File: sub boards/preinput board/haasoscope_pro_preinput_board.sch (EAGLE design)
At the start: 31 parts, among them J4 8pin, K1 G6K-2F-RF-T-TR03_DC5, K2 G6K-2F-RF-T-TR03_DC5, K3 TLP3475R_TP,F, K5 G6K-2F-RF-T-TR03_DC5, Q1 S8050, Q2 S8050, Q3 S8050

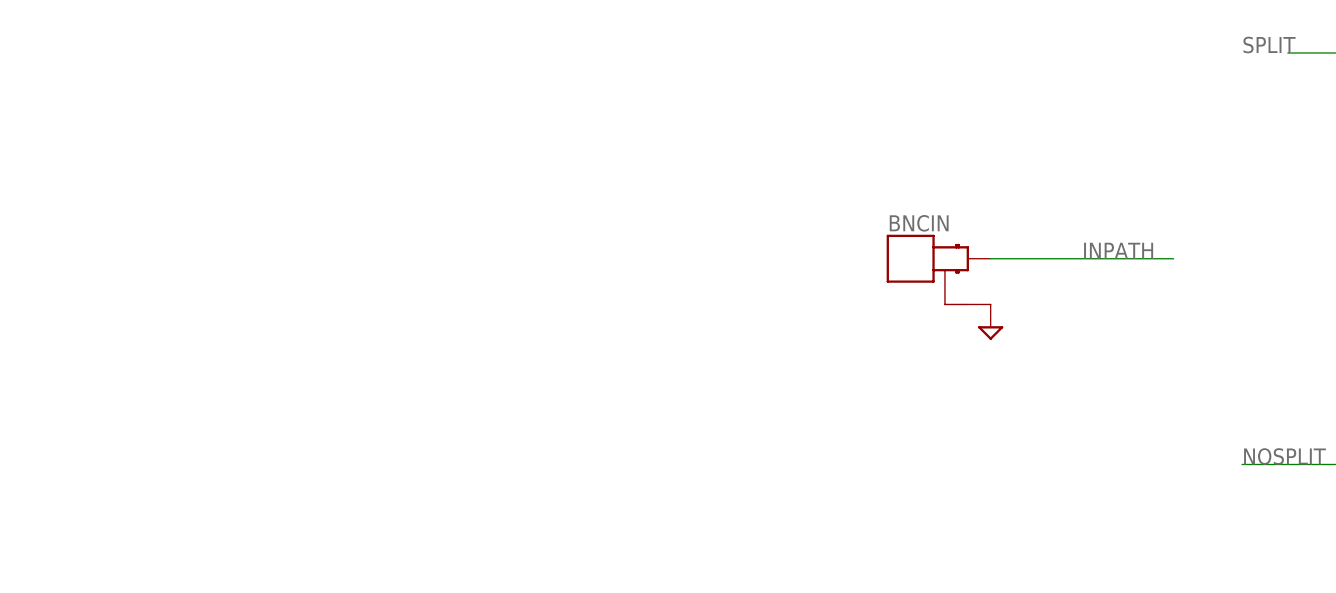
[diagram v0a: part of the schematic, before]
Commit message: Deemphasis filter
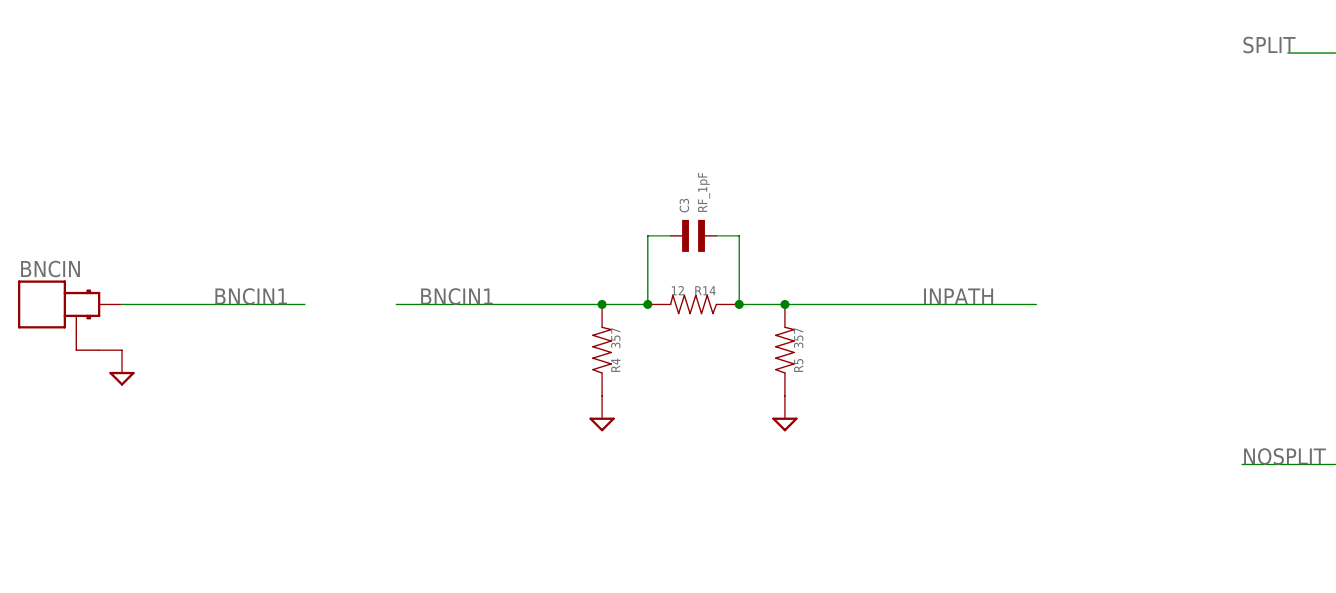
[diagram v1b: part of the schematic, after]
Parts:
- added C3: RF_1pF, MF_Passives:CAPACITOR_NP_0402
- added R14: 12, MF_Passives:RESISTOR_0402
- added R4, R5: 357, MF_Passives:RESISTOR_0402
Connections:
- new net BNCIN1: BNCIN.SIGNAL, C3.P$1, R14.P$2, R4.P$2
- net GND: now also R4.P$1, R5.P$1
- net INPATH: now also C3.P$2, R14.P$1, R5.P$2; no longer BNCIN.SIGNAL
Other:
- note added: "Pre-deemphasis pi attenuator -2.2dB low F, -1.2dB high F RC cutoff at ~350 MHz 50 Ohm"
- moved on the sheet: BNCIN
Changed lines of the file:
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@@
 <part name="K2" library="G6K-2F-RF-T-TR03_DC5" deviceset="G6K-2F-RF-T-TR03_DC5" device=""/>
 <part name="SUPPLY16" library="supply2" library_urn="urn:adsk.eagle:library:372" deviceset="GND" device=""/>
+<part name="SUPPLY21" library="supply2" library_urn="urn:adsk.eagle:library:372" deviceset="GND" device=""/>
+<part name="SUPPLY22" library="supply2" library_urn="urn:adsk.eagle:library:372" deviceset="GND" device=""/>
+<part name="R4" library="MF_Passives" deviceset="RESISTOR" device="_0402" value="357"/>
+<part name="R5" library="MF_Passives" deviceset="RESISTOR" device="_0402" value="357"/>
+<part name="R14" library="MF_Passives" deviceset="RESISTOR" device="_0402" value="12"/>
+<part name="C3" library="MF_Passives" deviceset="CAPACITOR_NP" device="_0402" value="RF_1pF">
+<attribute name="LCSC" value="C52923"/>
+</part>
 </parts>
 <sheets>
@@
 for CL05A105KA5NQNC</text>
 <text x="142.24" y="-73.66" size="1.778" layer="90">Inputs and controls</text>
+<text x="68.58" y="76.2" size="1.778" layer="90">Pre-deemphasis pi attenuator
+-2.2dB low F, -1.2dB high F
+RC cutoff at ~350 MHz
+50 Ohm</text>
 </plain>
 <instances>
@@
 <attribute name="VALUE" x="308.61" y="79.502" size="1.778" layer="96" rot="R180"/>
 </instance>
-<instance part="BNCIN" gate="G$1" x="101.6" y="66.04" smashed="yes">
-<attribute name="MPN" x="109.22" y="66.04" size="1.778" layer="96" display="off"/>
-<attribute name="NAME" x="97.79" y="69.088" size="1.778" layer="95" ratio="12"/>
-</instance>
-<instance part="SUPPLY2" gate="GND" x="109.22" y="58.42" smashed="yes" rot="MR0"/>
+<instance part="BNCIN" gate="G$1" x="5.08" y="60.96" smashed="yes">
+<attribute name="MPN" x="12.7" y="60.96" size="1.778" layer="96" display="off"/>
+<attribute name="NAME" x="1.27" y="64.008" size="1.778" layer="95" ratio="12"/>
+</instance>
+<instance part="SUPPLY2" gate="GND" x="12.7" y="53.34" smashed="yes" rot="MR0"/>
 <instance part="SUPPLY3" gate="GND" x="439.42" y="73.66" smashed="yes" rot="MR0"/>
 <instance part="SUPPLY4" gate="GND" x="256.54" y="-7.62" smashed="yes"/>
@@
 </instance>
 <instance part="SUPPLY16" gate="GND" x="429.26" y="-7.62" smashed="yes"/>
+<instance part="SUPPLY21" gate="GND" x="66.04" y="48.26" smashed="yes"/>
+<instance part="SUPPLY22" gate="GND" x="86.36" y="48.26" smashed="yes"/>
+<instance part="R4" gate="G$1" x="66.04" y="55.88" smashed="yes" rot="R180">
+<attribute name="NAME" x="67.056" y="53.34" size="1.016" layer="95" font="vector" rot="R90" align="top-left"/>
+<attribute name="VALUE" x="67.056" y="58.42" size="1.016" layer="96" font="vector" rot="R270"/>
+</instance>
+<instance part="R5" gate="G$1" x="86.36" y="55.88" smashed="yes" rot="R180">
+<attribute name="NAME" x="87.376" y="53.34" size="1.016" layer="95" font="vector" rot="R90" align="top-left"/>
+<attribute name="VALUE" x="87.376" y="58.42" size="1.016" layer="96" font="vector" rot="R270"/>
+</instance>
+<instance part="R14" gate="G$1" x="76.2" y="60.96" smashed="yes" rot="R270">
+<attribute name="NAME" x="78.74" y="61.976" size="1.016" layer="95" font="vector" rot="R180" align="top-left"/>
+<attribute name="VALUE" x="73.66" y="61.976" size="1.016" layer="96" font="vector"/>
+</instance>
+<instance part="C3" gate="G$1" x="76.2" y="68.58" smashed="yes" rot="R90">
+<attribute name="NAME" x="74.676" y="71.12" size="1.016" layer="95" font="vector" rot="R90" align="top-left"/>
+<attribute name="VALUE" x="77.724" y="71.12" size="1.016" layer="96" font="vector" rot="R90"/>
+<attribute name="LCSC" x="76.2" y="68.58" size="1.778" layer="96" rot="R90" display="off"/>
+</instance>
 </instances>
 <busses>
@@
 <pinref part="SUPPLY16" gate="GND" pin="GND"/>
 </segment>
+<segment>
+<pinref part="SUPPLY21" gate="GND" pin="GND"/>
+<pinref part="R4" gate="G$1" pin="P$1"/>
+</segment>
+<segment>
+<pinref part="SUPPLY22" gate="GND" pin="GND"/>
+<pinref part="R5" gate="G$1" pin="P$1"/>
+</segment>
 </net>
 <net name="VS+" class="0">
@@
 <net name="INPATH" class="0">
 <segment>
-<pinref part="BNCIN" gate="G$1" pin="SIGNAL"/>
-<wire x1="109.22" y1="66.04" x2="129.54" y2="66.04" width="0.1524" layer="91"/>
-<label x="119.38" y="66.04" size="1.778" layer="95"/>
-</segment>
-<segment>
 <wire x1="152.4" y1="2.54" x2="139.7" y2="2.54" width="0.1524" layer="91"/>
 <label x="142.24" y="2.54" size="1.778" layer="95"/>
 <pinref part="K1" gate="G$1" pin="COM_1"/>
+</segment>
+<segment>
+<label x="101.6" y="60.96" size="1.778" layer="95"/>
+<wire x1="81.28" y1="60.96" x2="86.36" y2="60.96" width="0.1524" layer="91"/>
+<wire x1="86.36" y1="60.96" x2="114.3" y2="60.96" width="0.1524" layer="91"/>
+<wire x1="81.28" y1="60.96" x2="81.28" y2="68.58" width="0.1524" layer="91"/>
+<pinref part="R5" gate="G$1" pin="P$2"/>
+<junction x="86.36" y="60.96"/>
+<pinref part="R14" gate="G$1" pin="P$1"/>
+<junction x="81.28" y="60.96"/>
+<pinref part="C3" gate="G$1" pin="P$2"/>
+<wire x1="81.28" y1="68.58" x2="78.74" y2="68.58" width="0.1524" layer="91"/>
 </segment>
 </net>
@@
 </segment>
 </net>
+<net name="BNCIN1" class="0">
+<segment>
+<pinref part="BNCIN" gate="G$1" pin="SIGNAL"/>
+<wire x1="12.7" y1="60.96" x2="33.02" y2="60.96" width="0.1524" layer="91"/>
+<label x="22.86" y="60.96" size="1.778" layer="95"/>
+</segment>
+<segment>
+<label x="45.72" y="60.96" size="1.778" layer="95"/>
+<wire x1="71.12" y1="60.96" x2="66.04" y2="60.96" width="0.1524" layer="91"/>
+<wire x1="66.04" y1="60.96" x2="43.18" y2="60.96" width="0.1524" layer="91"/>
+<wire x1="73.66" y1="68.58" x2="71.12" y2="68.58" width="0.1524" layer="91"/>
+<wire x1="71.12" y1="68.58" x2="71.12" y2="60.96" width="0.1524" layer="91"/>
+<pinref part="R4" gate="G$1" pin="P$2"/>
+<junction x="66.04" y="60.96"/>
+<pinref part="R14" gate="G$1" pin="P$2"/>
+<junction x="71.12" y="60.96"/>
+<pinref part="C3" gate="G$1" pin="P$1"/>
+</segment>
+</net>

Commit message: 27 pF
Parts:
- C3: value RF_1pF -> RF_27pF
- R14: value 12 -> 15
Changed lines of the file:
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@@
 <part name="R4" library="MF_Passives" deviceset="RESISTOR" device="_0402" value="357"/>
 <part name="R5" library="MF_Passives" deviceset="RESISTOR" device="_0402" value="357"/>
-<part name="R14" library="MF_Passives" deviceset="RESISTOR" device="_0402" value="12"/>
-<part name="C3" library="MF_Passives" deviceset="CAPACITOR_NP" device="_0402" value="RF_1pF">
+<part name="R14" library="MF_Passives" deviceset="RESISTOR" device="_0402" value="15"/>
+<part name="C3" library="MF_Passives" deviceset="CAPACITOR_NP" device="_0402" value="RF_27pF">
 <attribute name="LCSC" value="C52923"/>
 </part>
@@
 </instance>
 <instance part="C3" gate="G$1" x="76.2" y="68.58" smashed="yes" rot="R90">
-<attribute name="NAME" x="74.676" y="71.12" size="1.016" layer="95" font="vector" rot="R90" align="top-left"/>
-<attribute name="VALUE" x="77.724" y="71.12" size="1.016" layer="96" font="vector" rot="R90"/>
+<attribute name="NAME" x="78.74" y="70.104" size="1.016" layer="95" font="vector" align="top-left"/>
+<attribute name="VALUE" x="73.66" y="64.516" size="1.016" layer="96" font="vector"/>
 <attribute name="LCSC" x="76.2" y="68.58" size="1.778" layer="96" rot="R90" display="off"/>
 </instance>

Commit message: try low pass 1.25 and 2.5 GHz filters
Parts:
- added C4: 2pF, MF_Passives:CAPACITOR_NP_0402
- added C5, C6: 3pF, MF_Passives:CAPACITOR_NP_0402
- added C7: 4.3pF, MF_Passives:CAPACITOR_NP_0402
- added C8, C9: 6.2pF, MF_Passives:CAPACITOR_NP_0402
- added C80: 27pF, MF_Passives:CAPACITOR_NP_0402
- added INSMA1, INSMA2, INSMA3, OUTSMA1, OUTSMA2, OUTSMA3: out50, adafruit:SMACONNECTOR_EDGE
- added L1, L2: 3.9nH, Nordic_nRF:INDUCTOR_0402_N
- added L3: 2.7nH, Nordic_nRF:INDUCTOR_0402_N
- added L4, L5: 8.2nH, Nordic_nRF:INDUCTOR_0402_N
- added L6: 5.6nH, Nordic_nRF:INDUCTOR_0402_N
- added R242: 27, MF_Passives:RESISTOR_0402
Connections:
- removed net BNCIN1: BNCIN.SIGNAL, C3.P$1, R14.P$2, R4.P$2
- new net N$10: C8.P$1, L4.2, L5.1
- new net N$11: C9.P$1, L5.2, L6.1
- new net N$67: C80.P$1, R242.P$2
- new net N$8: C5.P$1, L1.2, L2.1
- new net N$9: C6.P$1, L2.2, L3.1
- new net SMAIN1: C3.P$1, INSMA1.ANT, R14.P$2, R4.P$2
- new net SMAIN2: C4.P$1, INSMA2.ANT, L1.1
- new net SMAIN3: C7.P$1, INSMA3.ANT, L4.1
- new net SMAOUT1: C3.P$2, OUTSMA1.ANT, R14.P$1, R5.P$2
- new net SMAOUT2: L3.2, OUTSMA2.ANT
- new net SMAOUT3: L6.2, OUTSMA3.ANT
- net GND: now also C4.P$2, C5.P$2, C6.P$2, C7.P$2, C8.P$2, C9.P$2, INSMA1.GND1, INSMA1.GND2, INSMA1.GND3, INSMA1.GND4, INSMA2.GND1, INSMA2.GND2, INSMA2.GND3, INSMA2.GND4, INSMA3.GND1, INSMA3.GND2, INSMA3.GND3, INSMA3.GND4, OUTSMA1.GND1, OUTSMA1.GND2, OUTSMA1.GND3, OUTSMA1.GND4, OUTSMA2.GND1, OUTSMA2.GND2, OUTSMA2.GND3, OUTSMA2.GND4, OUTSMA3.GND1, OUTSMA3.GND2, OUTSMA3.GND3, OUTSMA3.GND4
- net INPATH: now also BNCIN.SIGNAL; no longer C3.P$2, R14.P$1, R5.P$2
- net OUTSPLIT: now also C80.P$2
- net SPLIT: now also R242.P$1
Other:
- note added: "Chebyshev Lowpass Filter 1.25 GHz 6th order 50 Ohm 0.5dB ripple Pi: 4.394pF 7.944nH 6.637pF 8.363nH 6.305pF 5.536nH"
- note added: "Chebyshev Lowpass Filter 2.5 GHz 6th order 50 Ohm 0.5dB ripple Pi: 2.197pF 3.972nH 3.319pF 4.181nH 3.152pF 2.768nH"
- note removed: "RF relay"
- moved on the sheet: BNCIN, C3, OUTSPLIT, Q1, Q2, Q3, R10, R13, R14, R3, R4, R5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

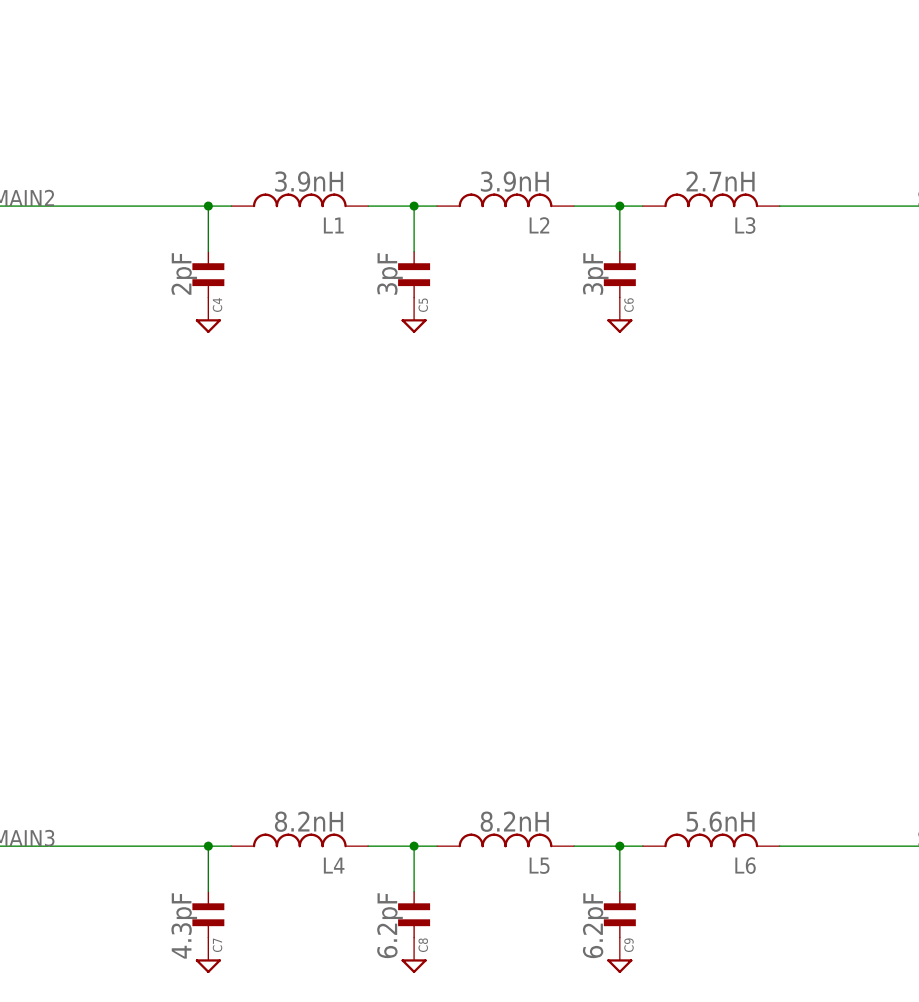
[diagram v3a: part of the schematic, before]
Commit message: update filter component values
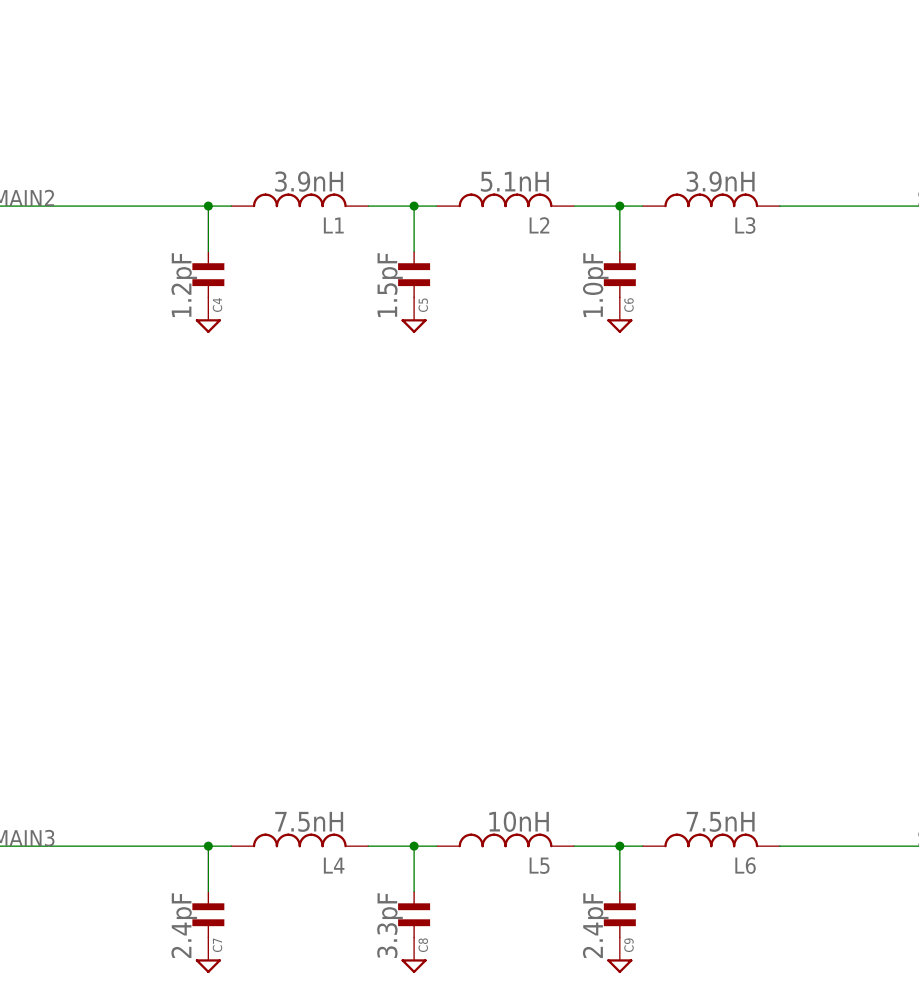
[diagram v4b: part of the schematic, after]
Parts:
- C4: value 2pF -> 1.2pF
- C5: value 3pF -> 1.5pF
- C6: value 3pF -> 1.0pF
- C7: value 4.3pF -> 2.4pF
- C8: value 6.2pF -> 3.3pF
- C9: value 6.2pF -> 2.4pF
- L2: value 3.9nH -> 5.1nH
- L3: value 2.7nH -> 3.9nH
- L4: value 8.2nH -> 7.5nH
- L5: value 8.2nH -> 10nH
- L6: value 5.6nH -> 7.5nH
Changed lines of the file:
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@@
 <part name="INSMA2" library="adafruit" deviceset="SMACONNECTOR" device="_EDGE" value="out50"/>
 <part name="SUPPLY25" library="supply2" library_urn="urn:adsk.eagle:library:372" deviceset="GND" device=""/>
-<part name="C4" library="MF_Passives" deviceset="CAPACITOR_NP" device="_0402" value="2pF">
+<part name="C4" library="MF_Passives" deviceset="CAPACITOR_NP" device="_0402" value="1.2pF">
 <attribute name="LCSC" value="C52923"/>
 </part>
 <part name="L1" library="Nordic_nRF" library_urn="urn:adsk.eagle:library:169009" deviceset="INDUCTOR" device="_0402_N" package3d_urn="urn:adsk.eagle:package:2593732/1" value="3.9nH"/>
-<part name="L2" library="Nordic_nRF" library_urn="urn:adsk.eagle:library:169009" deviceset="INDUCTOR" device="_0402_N" package3d_urn="urn:adsk.eagle:package:2593732/1" value="3.9nH"/>
-<part name="L3" library="Nordic_nRF" library_urn="urn:adsk.eagle:library:169009" deviceset="INDUCTOR" device="_0402_N" package3d_urn="urn:adsk.eagle:package:2593732/1" value="2.7nH"/>
-<part name="C5" library="MF_Passives" deviceset="CAPACITOR_NP" device="_0402" value="3pF">
+<part name="L2" library="Nordic_nRF" library_urn="urn:adsk.eagle:library:169009" deviceset="INDUCTOR" device="_0402_N" package3d_urn="urn:adsk.eagle:package:2593732/1" value="5.1nH"/>
+<part name="L3" library="Nordic_nRF" library_urn="urn:adsk.eagle:library:169009" deviceset="INDUCTOR" device="_0402_N" package3d_urn="urn:adsk.eagle:package:2593732/1" value="3.9nH"/>
+<part name="C5" library="MF_Passives" deviceset="CAPACITOR_NP" device="_0402" value="1.5pF">
 <attribute name="LCSC" value="C52923"/>
 </part>
-<part name="C6" library="MF_Passives" deviceset="CAPACITOR_NP" device="_0402" value="3pF">
+<part name="C6" library="MF_Passives" deviceset="CAPACITOR_NP" device="_0402" value="1.0pF">
 <attribute name="LCSC" value="C52923"/>
 </part>
@@
 <part name="INSMA3" library="adafruit" deviceset="SMACONNECTOR" device="_EDGE" value="out50"/>
 <part name="SUPPLY31" library="supply2" library_urn="urn:adsk.eagle:library:372" deviceset="GND" device=""/>
-<part name="C7" library="MF_Passives" deviceset="CAPACITOR_NP" device="_0402" value="4.3pF">
+<part name="C7" library="MF_Passives" deviceset="CAPACITOR_NP" device="_0402" value="2.4pF">
 <attribute name="LCSC" value="C52923"/>
 </part>
-<part name="L4" library="Nordic_nRF" library_urn="urn:adsk.eagle:library:169009" deviceset="INDUCTOR" device="_0402_N" package3d_urn="urn:adsk.eagle:package:2593732/1" value="8.2nH"/>
-<part name="L5" library="Nordic_nRF" library_urn="urn:adsk.eagle:library:169009" deviceset="INDUCTOR" device="_0402_N" package3d_urn="urn:adsk.eagle:package:2593732/1" value="8.2nH"/>
-<part name="L6" library="Nordic_nRF" library_urn="urn:adsk.eagle:library:169009" deviceset="INDUCTOR" device="_0402_N" package3d_urn="urn:adsk.eagle:package:2593732/1" value="5.6nH"/>
-<part name="C8" library="MF_Passives" deviceset="CAPACITOR_NP" device="_0402" value="6.2pF">
+<part name="L4" library="Nordic_nRF" library_urn="urn:adsk.eagle:library:169009" deviceset="INDUCTOR" device="_0402_N" package3d_urn="urn:adsk.eagle:package:2593732/1" value="7.5nH"/>
+<part name="L5" library="Nordic_nRF" library_urn="urn:adsk.eagle:library:169009" deviceset="INDUCTOR" device="_0402_N" package3d_urn="urn:adsk.eagle:package:2593732/1" value="10nH"/>
+<part name="L6" library="Nordic_nRF" library_urn="urn:adsk.eagle:library:169009" deviceset="INDUCTOR" device="_0402_N" package3d_urn="urn:adsk.eagle:package:2593732/1" value="7.5nH"/>
+<part name="C8" library="MF_Passives" deviceset="CAPACITOR_NP" device="_0402" value="3.3pF">
 <attribute name="LCSC" value="C52923"/>
 </part>
-<part name="C9" library="MF_Passives" deviceset="CAPACITOR_NP" device="_0402" value="6.2pF">
+<part name="C9" library="MF_Passives" deviceset="CAPACITOR_NP" device="_0402" value="2.4pF">
 <attribute name="LCSC" value="C52923"/>
 </part>
